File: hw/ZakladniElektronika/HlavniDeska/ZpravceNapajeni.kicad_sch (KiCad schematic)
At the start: 12 parts, among them Q10 Q_PMOS_DGS, Q13 Q_PMOS_DGS

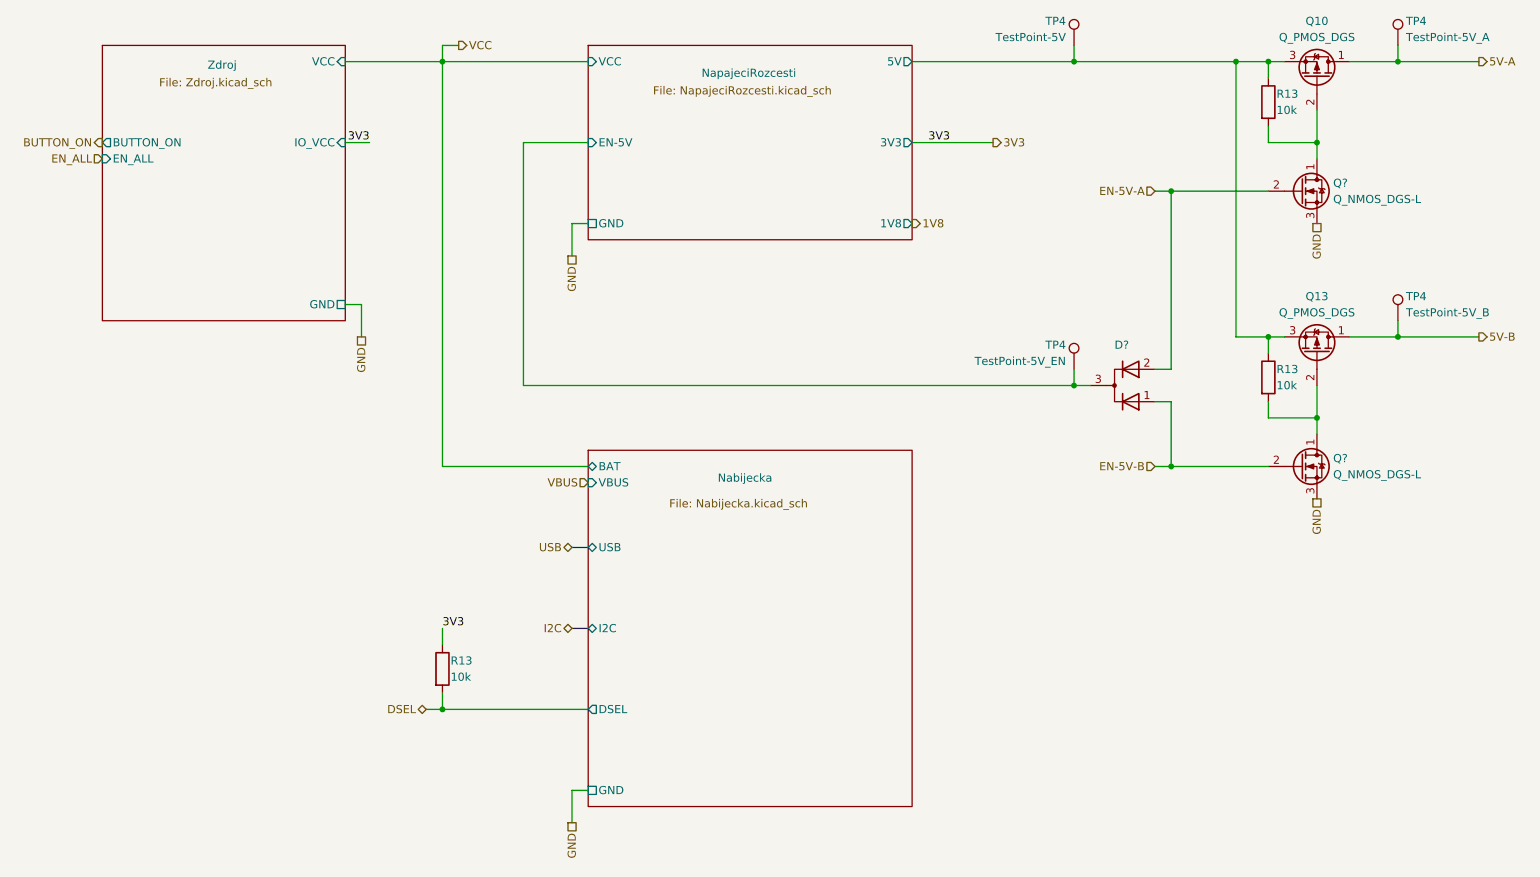
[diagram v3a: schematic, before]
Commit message: Výmněna ochrany baterie
Předchozí ochranný čip JLCPCB nemělo na skladě
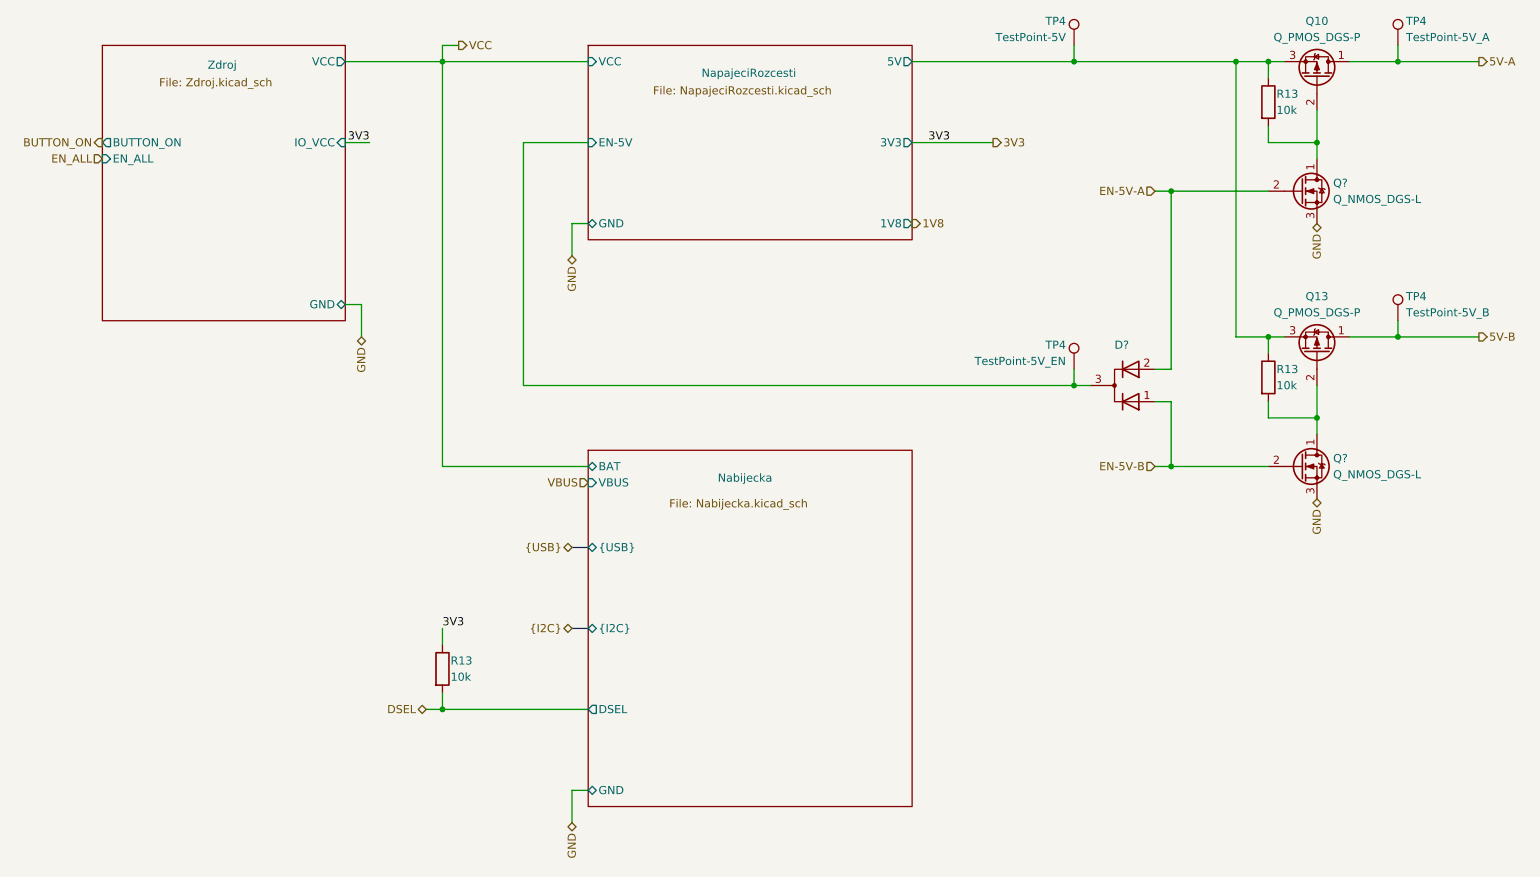
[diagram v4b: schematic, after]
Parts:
- Q10, Q13: value Q_PMOS_DGS -> Q_PMOS_DGS-P
- TP4: footprint (none) -> Connector_Pin:Pin_D0.9mm_L10.0mm_W2.4mm_FlatFork
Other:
- sheet Nabijecka ports: added {I2C}, {USB}; removed I2C, USB
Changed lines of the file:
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@@
     (effects (font (size 1.27 1.27)) (justify right bottom))
   )
-  (hierarchical_label "GND" (shape passive) (at 124.46 68.58 270) (fields_autoplaced)
-    (effects (font (size 1.27 1.27)) (justify right))
-  )
-  (hierarchical_label "GND" (shape passive) (at 124.46 157.48 270) (fields_autoplaced)
-    (effects (font (size 1.27 1.27)) (justify right))
-  )
-  (hierarchical_label "GND" (shape passive) (at 91.44 81.28 270) (fields_autoplaced)
+  (hierarchical_label "GND" (shape bidirectional) (at 124.46 68.58 270) (fields_autoplaced)
+    (effects (font (size 1.27 1.27)) (justify right))
+  )
+  (hierarchical_label "GND" (shape bidirectional) (at 124.46 157.48 270) (fields_autoplaced)
+    (effects (font (size 1.27 1.27)) (justify right))
+  )
+  (hierarchical_label "{I2C}" (shape bidirectional) (at 124.46 127 180) (fields_autoplaced)
+    (effects (font (size 1.27 1.27)) (justify right))
+  )
+  (hierarchical_label "GND" (shape bidirectional) (at 91.44 81.28 270) (fields_autoplaced)
     (effects (font (size 1.27 1.27)) (justify right))
   )
@@
     (effects (font (size 1.27 1.27)) (justify left))
   )
-  (hierarchical_label "GND" (shape passive) (at 241.3 63.5 270) (fields_autoplaced)
+  (hierarchical_label "{USB}" (shape bidirectional) (at 124.46 114.3 180) (fields_autoplaced)
+    (effects (font (size 1.27 1.27)) (justify right))
+  )
+  (hierarchical_label "GND" (shape bidirectional) (at 241.3 63.5 270) (fields_autoplaced)
     (effects (font (size 1.27 1.27)) (justify right))
   )
@@
     (effects (font (size 1.27 1.27)) (justify right))
   )
-  (hierarchical_label "USB" (shape bidirectional) (at 124.46 114.3 180) (fields_autoplaced)
-    (effects (font (size 1.27 1.27)) (justify right))
-  )
   (hierarchical_label "5V-B" (shape output) (at 266.7 81.28 0) (fields_autoplaced)
     (effects (font (size 1.27 1.27)) (justify left))
   )
-  (hierarchical_label "I2C" (shape bidirectional) (at 124.46 127 180) (fields_autoplaced)
-    (effects (font (size 1.27 1.27)) (justify right))
-  )
   (hierarchical_label "1V8" (shape output) (at 177.8 63.5 0) (fields_autoplaced)
     (effects (font (size 1.27 1.27)) (justify left))
@@
     (effects (font (size 1.27 1.27)) (justify right))
   )
-  (hierarchical_label "GND" (shape passive) (at 241.3 106.68 270) (fields_autoplaced)
+  (hierarchical_label "GND" (shape bidirectional) (at 241.3 106.68 270) (fields_autoplaced)
     (effects (font (size 1.27 1.27)) (justify right))
   )
@@
       (effects (font (size 1.27 1.27)) (justify left))
     )
-    (property "Footprint" "" (at 259.08 35.56 0)
+    (property "Footprint" "Connector_Pin:Pin_D0.9mm_L10.0mm_W2.4mm_FlatFork" (at 259.08 35.56 0)
       (effects (font (size 1.27 1.27)) hide)
     )
@@
       (effects (font (size 1.27 1.27)) (justify right))
     )
-    (property "Footprint" "" (at 208.28 35.56 0)
+    (property "Footprint" "Connector_Pin:Pin_D0.9mm_L10.0mm_W2.4mm_FlatFork" (at 208.28 35.56 0)
       (effects (font (size 1.27 1.27)) hide)
     )
@@
       (effects (font (size 1.27 1.27)) (justify left))
     )
-    (property "Footprint" "" (at 259.08 78.74 0)
+    (property "Footprint" "Connector_Pin:Pin_D0.9mm_L10.0mm_W2.4mm_FlatFork" (at 259.08 78.74 0)
       (effects (font (size 1.27 1.27)) hide)
     )
@@
       (effects (font (size 1.27 1.27)))
     )
-    (property "Value" "Q_PMOS_DGS" (at 241.3 77.47 90)
+    (property "Value" "Q_PMOS_DGS-P" (at 241.3 77.47 90)
       (effects (font (size 1.27 1.27)))
     )
@@
       (effects (font (size 1.27 1.27)))
     )
-    (property "Value" "Q_PMOS_DGS" (at 241.3 34.29 90)
+    (property "Value" "Q_PMOS_DGS-P" (at 241.3 34.29 90)
       (effects (font (size 1.27 1.27)))
     )
@@
       (effects (font (size 1.27 1.27)) (justify right))
     )
-    (property "Footprint" "" (at 208.28 86.36 0)
+    (property "Footprint" "Connector_Pin:Pin_D0.9mm_L10.0mm_W2.4mm_FlatFork" (at 208.28 86.36 0)
       (effects (font (size 1.27 1.27)) hide)
     )
@@
       (effects (font (size 1.27 1.27)) (justify right))
     )
-    (pin "GND" passive (at 127 63.5 180)
+    (pin "GND" bidirectional (at 127 63.5 180)
       (effects (font (size 1.27 1.27)) (justify left))
     )
@@
       (effects (font (size 1.27 1.27)) (justify left))
     )
-    (pin "I2C" bidirectional (at 127 127 180)
+    (pin "{I2C}" bidirectional (at 127 127 180)
       (effects (font (size 1.27 1.27)) (justify left))
     )
@@
       (effects (font (size 1.27 1.27)) (justify left))
     )
-    (pin "USB" bidirectional (at 127 114.3 180)
-      (effects (font (size 1.27 1.27)) (justify left))
-    )
-    (pin "GND" passive (at 127 152.4 180)
+    (pin "{USB}" bidirectional (at 127 114.3 180)
+      (effects (font (size 1.27 1.27)) (justify left))
+    )
+    (pin "GND" bidirectional (at 127 152.4 180)
       (effects (font (size 1.27 1.27)) (justify left))
     )
@@
       (effects (font (size 1.27 1.27)) (justify left top))
     )
-    (pin "VCC" input (at 88.9 38.1 0)
+    (pin "VCC" output (at 88.9 38.1 0)
       (effects (font (size 1.27 1.27)) (justify right))
     )
@@
       (effects (font (size 1.27 1.27)) (justify right))
     )
-    (pin "GND" passive (at 88.9 76.2 0)
-      (effects (font (size 1.27 1.27)) (justify right))
-    )
+    (pin "GND" bidirectional (at 88.9 76.2 0)
+      (effects (font (size 1.27 1.27)) (justify right))
+    )

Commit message: WIP
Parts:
- Q10, Q13: symbol Device:Q_PMOS_DGS -> RKL-Uncategorized:JMSL0302AU
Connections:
- net 5V-A: now also Q10.5 (D); no longer Q10.1 (D)
- net 5V-B: now also Q13.5 (D); no longer Q13.1 (D)
- net at Q?.1 (D), R13.2: now also Q13.4 (G); no longer Q13.2 (G)
- net at Q?.1 (D), R13.2: now also Q10.4 (G); no longer Q10.2 (G)
- net NapajeciRozcesti/5V renamed 5V-IN
- net 5V-IN: now also Q10.1 (S), Q10.2 (S), Q13.1 (S), Q13.2 (S)
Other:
- moved on the sheet: Q10, Q13
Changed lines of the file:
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@@
   (junction (at 254 81.28) (diameter 0) (color 0 0 0 0)
   )
-  (junction (at 104.14 38.1) (diameter 0) (color 0 0 0 0)
+  (junction (at 101.6 38.1) (diameter 0) (color 0 0 0 0)
   )
   (junction (at 218.44 101.6) (diameter 0) (color 0 0 0 0)
@@
     (stroke (width 0) (type default))
   )
-  (wire (pts (xy 104.14 35.56) (xy 106.68 35.56))
+  (wire (pts (xy 101.6 35.56) (xy 104.14 35.56))
+    (stroke (width 0) (type default))
+  )
+  (wire (pts (xy 91.44 81.28) (xy 91.44 76.2))
+    (stroke (width 0) (type default))
+  )
+  (wire (pts (xy 241.3 93.98) (xy 241.3 96.52))
+    (stroke (width 0) (type default))
+  )
+  (wire (pts (xy 254 81.28) (xy 246.38 81.28))
+    (stroke (width 0) (type default))
+  )
+  (wire (pts (xy 114.3 50.8) (xy 127 50.8))
+    (stroke (width 0) (type default))
+  )
+  (wire (pts (xy 228.6 38.1) (xy 228.6 81.28))
+    (stroke (width 0) (type default))
+  )
+  (wire (pts (xy 233.68 81.28) (xy 233.68 83.82))
+    (stroke (width 0) (type default))
+  )
+  (wire (pts (xy 266.7 81.28) (xy 254 81.28))
+    (stroke (width 0) (type default))
+  )
+  (wire (pts (xy 215.9 58.42) (xy 218.44 58.42))
+    (stroke (width 0) (type default))
+  )
+  (wire (pts (xy 241.3 88.9) (xy 241.3 93.98))
+    (stroke (width 0) (type default))
+  )
+  (wire (pts (xy 218.44 101.6) (xy 233.68 101.6))
+    (stroke (width 0) (type default))
+  )
+  (wire (pts (xy 177.8 38.1) (xy 203.2 38.1))
+    (stroke (width 0) (type default))
+  )
+  (wire (pts (xy 254 38.1) (xy 246.38 38.1))
+    (stroke (width 0) (type default))
+  )
+  (wire (pts (xy 254 81.28) (xy 254 78.74))
+    (stroke (width 0) (type default))
+  )
+  (wire (pts (xy 91.44 76.2) (xy 88.9 76.2))
     (stroke (width 0) (type default))
   )
@@
     (stroke (width 0) (type default))
   )
-  (wire (pts (xy 91.44 81.28) (xy 91.44 76.2))
-    (stroke (width 0) (type default))
-  )
-  (wire (pts (xy 241.3 93.98) (xy 241.3 96.52))
-    (stroke (width 0) (type default))
-  )
-  (wire (pts (xy 254 81.28) (xy 246.38 81.28))
-    (stroke (width 0) (type default))
-  )
-  (wire (pts (xy 116.84 50.8) (xy 127 50.8))
-    (stroke (width 0) (type default))
-  )
-  (wire (pts (xy 228.6 38.1) (xy 228.6 81.28))
-    (stroke (width 0) (type default))
-  )
-  (wire (pts (xy 233.68 81.28) (xy 233.68 83.82))
-    (stroke (width 0) (type default))
-  )
-  (wire (pts (xy 266.7 81.28) (xy 254 81.28))
-    (stroke (width 0) (type default))
-  )
-  (wire (pts (xy 215.9 58.42) (xy 218.44 58.42))
-    (stroke (width 0) (type default))
-  )
-  (wire (pts (xy 218.44 101.6) (xy 233.68 101.6))
-    (stroke (width 0) (type default))
-  )
-  (wire (pts (xy 177.8 38.1) (xy 203.2 38.1))
-    (stroke (width 0) (type default))
-  )
-  (wire (pts (xy 241.3 88.9) (xy 241.3 93.98))
-    (stroke (width 0) (type default))
-  )
-  (wire (pts (xy 254 38.1) (xy 246.38 38.1))
-    (stroke (width 0) (type default))
-  )
-  (wire (pts (xy 254 81.28) (xy 254 78.74))
-    (stroke (width 0) (type default))
-  )
-  (wire (pts (xy 91.44 76.2) (xy 88.9 76.2))
-    (stroke (width 0) (type default))
-  )
-  (wire (pts (xy 88.9 38.1) (xy 104.14 38.1))
+  (wire (pts (xy 88.9 38.1) (xy 101.6 38.1))
     (stroke (width 0) (type default))
   )
@@
     (stroke (width 0) (type default))
   )
-  (wire (pts (xy 104.14 38.1) (xy 104.14 35.56))
+  (wire (pts (xy 101.6 38.1) (xy 101.6 35.56))
     (stroke (width 0) (type default))
   )
@@
     (stroke (width 0) (type default))
   )
-  (wire (pts (xy 104.14 38.1) (xy 127 38.1))
-    (stroke (width 0) (type default))
-  )
-  (wire (pts (xy 104.14 38.1) (xy 104.14 101.6))
+  (wire (pts (xy 101.6 38.1) (xy 127 38.1))
+    (stroke (width 0) (type default))
+  )
+  (wire (pts (xy 101.6 38.1) (xy 101.6 101.6))
     (stroke (width 0) (type default))
   )
@@
     (stroke (width 0) (type default))
   )
-  (wire (pts (xy 203.2 88.9) (xy 116.84 88.9))
+  (wire (pts (xy 203.2 88.9) (xy 114.3 88.9))
     (stroke (width 0) (type default))
   )
@@
     (stroke (width 0) (type default))
   )
-  (wire (pts (xy 127 101.6) (xy 104.14 101.6))
+  (wire (pts (xy 127 101.6) (xy 101.6 101.6))
     (stroke (width 0) (type default))
   )
@@
     (stroke (width 0) (type default))
   )
-  (wire (pts (xy 116.84 50.8) (xy 116.84 88.9))
+  (wire (pts (xy 114.3 50.8) (xy 114.3 88.9))
     (stroke (width 0) (type default))
   )
@@
     (effects (font (size 1.27 1.27)) (justify left bottom))
   )
+  (label "5V-IN" (at 215.9 38.1 0) (fields_autoplaced)
+    (effects (font (size 1.27 1.27)) (justify left bottom))
+  )
   (label "3V3" (at 92.71 50.8 180) (fields_autoplaced)
     (effects (font (size 1.27 1.27)) (justify right bottom))
@@
     (effects (font (size 1.27 1.27)) (justify left))
   )
-  (hierarchical_label "VCC" (shape output) (at 106.68 35.56 0) (fields_autoplaced)
+  (hierarchical_label "VCC" (shape output) (at 104.14 35.56 0) (fields_autoplaced)
     (effects (font (size 1.27 1.27)) (justify left))
   )
@@
     )
   )
-  (symbol (lib_id "Device:Q_PMOS_DGS") (at 241.3 83.82 270) (mirror x) (unit 1)
-    (in_bom yes) (on_board yes) (dnp no)
-    (property "Reference" "Q13" (at 241.3 74.93 90)
+  (symbol (lib_id "RKL-Uncategorized:JMSL0302AU") (at 241.3 81.28 0) (mirror y) (unit 1)
+    (in_bom yes) (on_board yes) (dnp no)
+    (property "Reference" "Q13" (at 241.3 74.93 0)
       (effects (font (size 1.27 1.27)))
     )
-    (property "Value" "Q_PMOS_DGS-P" (at 241.3 77.47 90)
+    (property "Value" "Q_PMOS_DGS-P" (at 241.3 77.47 0)
       (effects (font (size 1.27 1.27)))
     )
-    (property "Footprint" "Package_SON:Diodes_PowerDI3333-8" (at 243.84 78.74 0)
-      (effects (font (size 1.27 1.27)) hide)
-    )
-    (property "Datasheet" "https://datasheet.lcsc.com/lcsc/2109070930_Jiangsu-JieJie-Microelectronics-JMSL0302AU_C2890409.pdf" (at 241.3 83.82 0)
-      (effects (font (size 1.27 1.27)) hide)
-    )
-    (property "LCSC" "C2890409" (at 241.3 83.82 90)
-      (effects (font (size 1.27 1.27)) hide)
-    )
-    (property "Basic/Extended" "E" (at 241.3 83.82 0)
-      (effects (font (size 1.27 1.27)) hide)
-    )
-    (property "JLCPCB_CORRECTION" "" (at 241.3 83.82 0)
+    (property "Footprint" "Package_SON:Diodes_PowerDI3333-8" (at 241.3 78.232 0)
+      (effects (font (size 1.27 1.27)) hide)
+    )
+    (property "Datasheet" "https://datasheet.lcsc.com/lcsc/2109070930_Jiangsu-JieJie-Microelectronics-JMSL0302AU_C2890409.pdf" (at 241.3 78.232 0)
+      (effects (font (size 1.27 1.27)) hide)
+    )
+    (property "LCSC" "C2890409" (at 241.3 81.28 90)
+      (effects (font (size 1.27 1.27)) hide)
+    )
+    (property "Basic/Extended" "E" (at 241.3 81.28 0)
+      (effects (font (size 1.27 1.27)) hide)
+    )
+    (property "JLCPCB_CORRECTION" "" (at 241.3 81.28 0)
       (effects (font (size 1.27 1.27)) hide)
     )
@@
     (pin "2")
     (pin "3")
+    (pin "4")
+    (pin "5")
     (instances
       (project "ZakladniElektronika"
@@
     )
   )
-  (symbol (lib_id "Device:Q_PMOS_DGS") (at 241.3 40.64 270) (mirror x) (unit 1)
-    (in_bom yes) (on_board yes) (dnp no)
-    (property "Reference" "Q10" (at 241.3 31.75 90)
+  (symbol (lib_id "RKL-Uncategorized:JMSL0302AU") (at 241.3 38.1 0) (mirror y) (unit 1)
+    (in_bom yes) (on_board yes) (dnp no)
+    (property "Reference" "Q10" (at 241.3 31.75 0)
       (effects (font (size 1.27 1.27)))
     )
-    (property "Value" "Q_PMOS_DGS-P" (at 241.3 34.29 90)
+    (property "Value" "Q_PMOS_DGS-P" (at 241.3 34.29 0)
       (effects (font (size 1.27 1.27)))
     )
-    (property "Footprint" "Package_SON:Diodes_PowerDI3333-8" (at 243.84 35.56 0)
-      (effects (font (size 1.27 1.27)) hide)
-    )
-    (property "Datasheet" "https://datasheet.lcsc.com/lcsc/2109070930_Jiangsu-JieJie-Microelectronics-JMSL0302AU_C2890409.pdf" (at 241.3 40.64 0)
-      (effects (font (size 1.27 1.27)) hide)
-    )
-    (property "LCSC" "C2890409" (at 241.3 40.64 90)
-      (effects (font (size 1.27 1.27)) hide)
-    )
-    (property "Basic/Extended" "E" (at 241.3 40.64 0)
-      (effects (font (size 1.27 1.27)) hide)
-    )
-    (property "JLCPCB_CORRECTION" "" (at 241.3 40.64 0)
+    (property "Footprint" "Package_SON:Diodes_PowerDI3333-8" (at 241.3 35.052 0)
+      (effects (font (size 1.27 1.27)) hide)
+    )
+    (property "Datasheet" "https://datasheet.lcsc.com/lcsc/2109070930_Jiangsu-JieJie-Microelectronics-JMSL0302AU_C2890409.pdf" (at 241.3 35.052 0)
+      (effects (font (size 1.27 1.27)) hide)
+    )
+    (property "LCSC" "C2890409" (at 241.3 38.1 90)
+      (effects (font (size 1.27 1.27)) hide)
+    )
+    (property "Basic/Extended" "E" (at 241.3 38.1 0)
+      (effects (font (size 1.27 1.27)) hide)
+    )
+    (property "JLCPCB_CORRECTION" "" (at 241.3 38.1 0)
       (effects (font (size 1.27 1.27)) hide)
     )
@@
     (pin "2")
     (pin "3")
-    (instances
-      (project "ZakladniElektronika"
+    (pin "4")
+    (pin "5")
+    (instances
+      (project "ZakladniElektronika"

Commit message: PCB
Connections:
- net EN-5V-A: now also D?.1 (K); no longer D?.2 (K)
- net EN-5V-B: now also D?.2 (K); no longer D?.1 (K)
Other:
- moved on the sheet: D?
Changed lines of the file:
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@@
     (effects (font (size 1.27 1.27)) (justify right))
   )
-  (symbol (lib_id "Device:D_Dual_CommonCathode_AAK_Parallel") (at 210.82 88.9 180) (unit 1)
+  (symbol (lib_id "Device:D_Dual_CommonCathode_AAK_Parallel") (at 210.82 88.9 0) (mirror y) (unit 1)
     (in_bom yes) (on_board yes) (dnp no)
-    (property "Reference" "D?" (at 209.55 82.55 0)
+    (property "Reference" "D?" (at 208.28 83.82 0)
       (effects (font (size 1.27 1.27)) (justify right))
     )
-    (property "Value" "D_Dual_CommonCathode_AAK_Parallel" (at 212.09 130.81 90)
+    (property "Value" "D_Dual_CommonCathode_AAK_Parallel" (at 212.09 46.99 90)
       (effects (font (size 1.27 1.27)) (justify right) hide)
     )

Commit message: AHS-V1
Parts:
- Q10, Q13: JLCPCB_CORRECTION (none) -> 0;0;-90
- Q? (x2): JLCPCB_CORRECTION (none) -> 0;0;180
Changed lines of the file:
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@@
       (effects (font (size 1.27 1.27)) hide)
     )
-    (property "JLCPCB_CORRECTION" "" (at 238.76 101.6 0)
+    (property "JLCPCB_CORRECTION" "0;0;180" (at 238.76 101.6 0)
       (effects (font (size 1.27 1.27)) hide)
     )
@@
       (effects (font (size 1.27 1.27)) hide)
     )
-    (property "JLCPCB_CORRECTION" "" (at 241.3 81.28 0)
+    (property "JLCPCB_CORRECTION" "0;0;-90" (at 241.3 81.28 0)
       (effects (font (size 1.27 1.27)) hide)
     )
@@
       (effects (font (size 1.27 1.27)) hide)
     )
-    (property "JLCPCB_CORRECTION" "" (at 241.3 38.1 0)
+    (property "JLCPCB_CORRECTION" "0;0;-90" (at 241.3 38.1 0)
       (effects (font (size 1.27 1.27)) hide)
     )
@@
       (effects (font (size 1.27 1.27)) hide)
     )
-    (property "JLCPCB_CORRECTION" "" (at 238.76 58.42 0)
-      (effects (font (size 1.27 1.27)) hide)
-    )
+    (property "JLCPCB_CORRECTION" "0;0;180" (at 238.76 58.42 0)
+      (effects (font (size 1.27 1.27)) hide)
+    )

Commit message: KiCad V8
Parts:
- renumbered R13 to R1, R13 to R23, R13 to R32, TP4 to TP10, TP4 to TP11, TP4 to TP8, TP4 to TP9
